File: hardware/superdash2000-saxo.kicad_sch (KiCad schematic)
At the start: 19 parts, among them IC1 MAX4617CPE+, J1 Molex 34691-0161, U1 L7805, U1 TLV2372

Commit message: hardware: Fix annotations
Signed-off-by: Thomas Antonini <antonini.thomas@gmail.com>
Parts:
- renumbered U1 to U2
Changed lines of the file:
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@@
   (symbol (lib_name "GND_1") (lib_id "power:GND") (at 154.94 41.91 0) (unit 1)
     (in_bom yes) (on_board yes) (fields_autoplaced)
-    (property "Reference" "#PWR?" (id 0) (at 154.94 48.26 0)
+    (property "Reference" "#PWR06" (id 0) (at 154.94 48.26 0)
       (effects (font (size 1.27 1.27)) hide)
     )
@@
   (symbol (lib_id "Amplifier_Operational:TLV2372") (at 72.39 113.03 0) (unit 3)
     (in_bom yes) (on_board yes) (fields_autoplaced)
-    (property "Reference" "U1" (id 0) (at 71.12 111.7599 0)
+    (property "Reference" "U2" (id 0) (at 71.12 111.7599 0)
       (effects (font (size 1.27 1.27)) (justify left))
     )
@@
   (symbol (lib_name "GND_3") (lib_id "power:GND") (at 109.22 111.76 0) (unit 1)
     (in_bom yes) (on_board yes) (fields_autoplaced)
-    (property "Reference" "#PWR?" (id 0) (at 109.22 118.11 0)
+    (property "Reference" "#PWR04" (id 0) (at 109.22 118.11 0)
       (effects (font (size 1.27 1.27)) hide)
     )
@@
   (symbol (lib_name "GND_5") (lib_id "power:GND") (at 109.22 151.13 0) (unit 1)
     (in_bom yes) (on_board yes) (fields_autoplaced)
-    (property "Reference" "#PWR?" (id 0) (at 109.22 157.48 0)
+    (property "Reference" "#PWR05" (id 0) (at 109.22 157.48 0)
       (effects (font (size 1.27 1.27)) hide)
     )
@@
   (symbol (lib_name "GND_4") (lib_id "power:GND") (at 195.58 137.16 0) (unit 1)
     (in_bom yes) (on_board yes) (fields_autoplaced)
-    (property "Reference" "#PWR?" (id 0) (at 195.58 143.51 0)
+    (property "Reference" "#PWR07" (id 0) (at 195.58 143.51 0)
       (effects (font (size 1.27 1.27)) hide)
     )
@@
   (symbol (lib_name "GND_2") (lib_id "power:GND") (at 69.85 120.65 0) (unit 1)
     (in_bom yes) (on_board yes) (fields_autoplaced)
-    (property "Reference" "#PWR?" (id 0) (at 69.85 127 0)
+    (property "Reference" "#PWR03" (id 0) (at 69.85 127 0)
       (effects (font (size 1.27 1.27)) hide)
     )
@@
   (symbol (lib_id "power:+BATT") (at 154.94 26.67 0) (unit 1)
     (in_bom yes) (on_board yes) (fields_autoplaced)
-    (property "Reference" "#PWR1" (id 0) (at 154.94 30.48 0)
+    (property "Reference" "#PWR01" (id 0) (at 154.94 30.48 0)
       (effects (font (size 1.27 1.27)) hide)
     )
@@
   (symbol (lib_id "power:+BATT") (at 81.28 64.77 0) (unit 1)
     (in_bom yes) (on_board yes) (fields_autoplaced)
-    (property "Reference" "#PWR1" (id 0) (at 81.28 68.58 0)
+    (property "Reference" "#PWR0103" (id 0) (at 81.28 68.58 0)
       (effects (font (size 1.27 1.27)) hide)
     )
@@
   (symbol (lib_id "power:+BATT") (at 69.85 105.41 0) (unit 1)
     (in_bom yes) (on_board yes) (fields_autoplaced)
-    (property "Reference" "#PWR?" (id 0) (at 69.85 109.22 0)
+    (property "Reference" "#PWR02" (id 0) (at 69.85 109.22 0)
       (effects (font (size 1.27 1.27)) hide)
     )
@@
   (symbol (lib_id "Amplifier_Operational:TLV2372") (at 92.71 93.98 0) (unit 1)
     (in_bom yes) (on_board yes) (fields_autoplaced)
-    (property "Reference" "U1" (id 0) (at 92.71 83.82 0))
+    (property "Reference" "U2" (id 0) (at 92.71 83.82 0))
     (property "Value" "TLV2372" (id 1) (at 92.71 86.36 0))
     (property "Footprint" "" (id 2) (at 92.71 93.98 0)
@@
   (symbol (lib_id "Amplifier_Operational:TLV2372") (at 92.71 133.35 0) (unit 2)
     (in_bom yes) (on_board yes) (fields_autoplaced)
-    (property "Reference" "U1" (id 0) (at 92.71 123.19 0))
+    (property "Reference" "U2" (id 0) (at 92.71 123.19 0))
     (property "Value" "TLV2372" (id 1) (at 92.71 125.73 0))
     (property "Footprint" "" (id 2) (at 92.71 133.35 0)
@@
   (symbol_instances
     (path "/b87c930c-8d22-4000-a82f-ac742bad5f6a"
-      (reference "#PWR1") (unit 1) (value "+BATT") (footprint "")
-    )
-    (path "/bfcc77a0-ee67-4af0-9e4b-c64f7ccc8208"
-      (reference "#PWR1") (unit 1) (value "+BATT") (footprint "")
+      (reference "#PWR01") (unit 1) (value "+BATT") (footprint "")
+    )
+    (path "/dca402e7-0e77-45e9-a01b-7f7133721d95"
+      (reference "#PWR02") (unit 1) (value "+BATT") (footprint "")
+    )
+    (path "/a55a6c63-efeb-4a39-b005-db7246ff05b2"
+      (reference "#PWR03") (unit 1) (value "GND") (footprint "")
+    )
+    (path "/44a14783-b732-4cad-b4e3-6acdd52fd22f"
+      (reference "#PWR04") (unit 1) (value "GND") (footprint "")
+    )
+    (path "/4c0b9cd9-ca22-4581-9004-f5bcc462bbf4"
+      (reference "#PWR05") (unit 1) (value "GND") (footprint "")
+    )
+    (path "/2c2c0160-d229-41a2-b822-4cf1420ec8e9"
+      (reference "#PWR06") (unit 1) (value "GND") (footprint "")
+    )
+    (path "/7c43fb8d-99fb-43c3-9bcb-9181569a93c6"
+      (reference "#PWR07") (unit 1) (value "GND") (footprint "")
     )
     (path "/091fa7fe-31f2-4bc7-b9ae-103378e7ecef"
@@
       (reference "#PWR0102") (unit 1) (value "GND") (footprint "")
     )
+    (path "/bfcc77a0-ee67-4af0-9e4b-c64f7ccc8208"
+      (reference "#PWR0103") (unit 1) (value "+BATT") (footprint "")
+    )
     (path "/d452a94e-41da-4920-9425-e3d186a49a40"
       (reference "#PWR0104") (unit 1) (value "+5V") (footprint "")
@@
       (reference "#PWR0106") (unit 1) (value "GND") (footprint "")
     )
-    (path "/2c2c0160-d229-41a2-b822-4cf1420ec8e9"
-      (reference "#PWR?") (unit 1) (value "GND") (footprint "")
-    )
-    (path "/44a14783-b732-4cad-b4e3-6acdd52fd22f"
-      (reference "#PWR?") (unit 1) (value "GND") (footprint "")
-    )
-    (path "/4c0b9cd9-ca22-4581-9004-f5bcc462bbf4"
-      (reference "#PWR?") (unit 1) (value "GND") (footprint "")
-    )
-    (path "/7c43fb8d-99fb-43c3-9bcb-9181569a93c6"
-      (reference "#PWR?") (unit 1) (value "GND") (footprint "")
-    )
-    (path "/a55a6c63-efeb-4a39-b005-db7246ff05b2"
-      (reference "#PWR?") (unit 1) (value "GND") (footprint "")
-    )
-    (path "/dca402e7-0e77-45e9-a01b-7f7133721d95"
-      (reference "#PWR?") (unit 1) (value "+BATT") (footprint "")
-    )
     (path "/65c02b6a-4170-4a63-9193-eec01920d5e8"
       (reference "A1") (unit 1) (value "Arduino_Nano_Every") (footprint "Module:Arduino_Nano")
@@
     )
     (path "/dd5c3b2c-bf9a-4210-9e80-91b487d16ffc"
-      (reference "U1") (unit 1) (value "TLV2372") (footprint "")
+      (reference "U2") (unit 1) (value "TLV2372") (footprint "")
     )
     (path "/decc528c-3d97-4a7b-9669-34ab28ca3491"
-      (reference "U1") (unit 2) (value "TLV2372") (footprint "")
+      (reference "U2") (unit 2) (value "TLV2372") (footprint "")
     )
     (path "/37d731ac-aa73-4d1a-b688-0abbd56fee75"
-      (reference "U1") (unit 3) (value "TLV2372") (footprint "")
-    )
-  )
+      (reference "U2") (unit 3) (value "TLV2372") (footprint "")
+    )
+  )

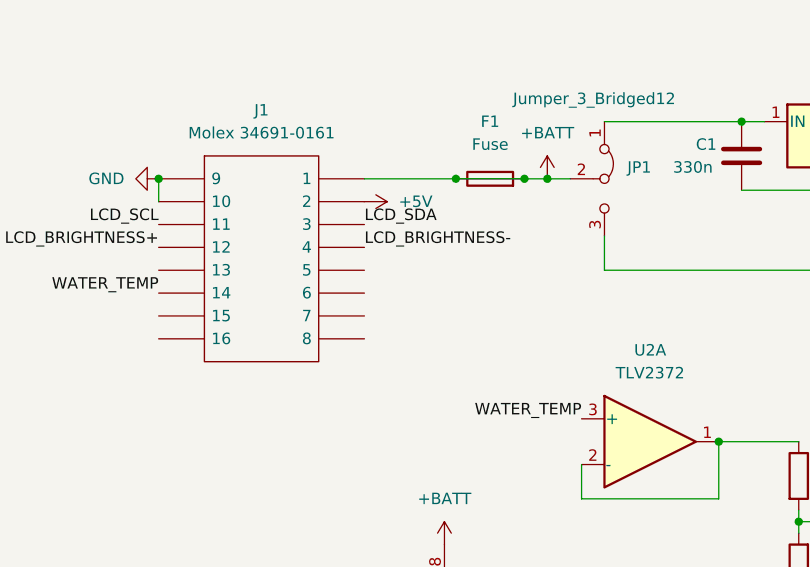
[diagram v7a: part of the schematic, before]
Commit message: hardware: Add missing DIMMER label on connector
Signed-off-by: Thomas Antonini <antonini.thomas@gmail.com>
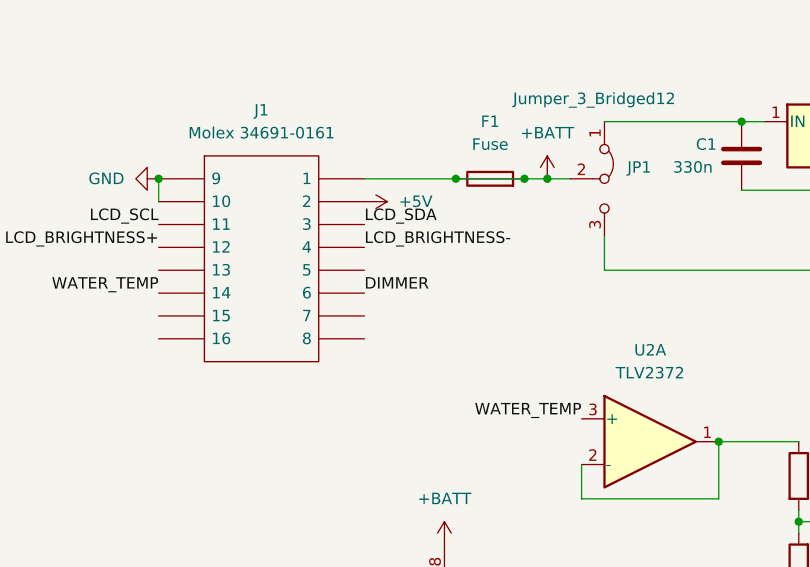
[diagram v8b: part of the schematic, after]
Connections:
- net DIMMER: now also J1.6
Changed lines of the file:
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@@
+    (effects (font (size 1.27 1.27)) (justify left bottom))
+  )
+  (label "DIMMER" (at 60.96 77.47 0)
     (effects (font (size 1.27 1.27)) (justify left bottom))
   )
